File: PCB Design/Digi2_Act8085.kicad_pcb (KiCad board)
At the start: 2 copper layers, 27 parts, among them U1 8085A, U10 8255, U2 Barrel_Jack, U3 L7805, U4 2764, U5 CY6264, U6 74LS373, U7 74LS138, U8 8255, U9 8255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

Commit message: Initial
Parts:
- moved C12 73.7 mm to (141.4, 113.5)
- moved U7 73.7 mm to (172.7, 94.7)
- moved Y1 73.7 mm to (141.4, 101.2)
- moved C2 73.7 mm to (155.2, 96.8)
- moved C4 73.7 mm to (174.8, 122.7)
- moved C5 73.7 mm to (200.5, 111.4)
- moved C6 73.7 mm to (229.1, 111.5)
- moved C9 73.7 mm to (188.9, 100.1)
- moved U1 73.7 mm to (150.1, 101.5)
- moved U4 73.7 mm to (224.7, 116.6)
- moved U5 73.7 mm to (195.3, 116.6)
- moved U8 73.7 mm to (193.4, 105.6)
- moved C3 73.7 mm to (174.0, 89.6)
- moved U6 73.7 mm to (173.2, 126.6)
- moved C7 72.3 mm to (188.8, 48.0)
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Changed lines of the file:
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@@
 	(footprint "Capacitor_THT:C_Disc_D4.3mm_W1.9mm_P5.00mm"
 		(layer "F.Cu")
-		(at 82.81 83.425)
+		(at 155.245 96.8)
 		(descr "C, Disc series, Radial, pin pitch=5.00mm, , diameter*width=4.3*1.9mm^2, Capacitor, http://www.vishay.com/docs/45233/krseries.pdf")
 		(tags "C Disc series Radial pin pitch 5.00mm  diameter 4.3mm width 1.9mm Capacitor")
@@
 	(footprint "Crystal:Crystal_HC49-U_Vertical"
 		(layer "F.Cu")
-		(at 68.925 87.795 -90)
+		(at 141.36 101.17 -90)
 		(descr "Crystal THT HC-49/U http://5hertz.com/pdfs/04404_D.pdf")
 		(tags "THT crystalHC-49/U")
@@
 	(footprint "Package_DIP:DIP-16_W7.62mm_Socket"
 		(layer "F.Cu")
-		(at 100.24 81.36)
+		(at 172.675 94.735)
 		(descr "16-lead though-hole mounted DIP package, row spacing 7.62 mm (300 mils), Socket")
 		(tags "THT DIP DIL PDIP 2.54mm 7.62mm 300mil Socket")
@@
 	(footprint "Package_DIP:DIP-20_W7.62mm_Socket"
 		(layer "F.Cu")
-		(at 100.79 113.27)
+		(at 173.225 126.645)
 		(descr "20-lead though-hole mounted DIP package, row spacing 7.62 mm (300 mils), Socket")
 		(tags "THT DIP DIL PDIP 2.54mm 7.62mm 300mil Socket")
 		(property "Reference" "U6"
-			(at 8.37 -2.72 360)
+			(at 8.37 -2.72 0)
 			(layer "F.SilkS")
 			(effects
@@
 		)
 		(property "Value" "74LS373"
-			(at 7.945 26.37 360)
+			(at 7.945 26.37 0)
 			(layer "F.Fab")
 			(effects
@@
 		)
 		(fp_text user "${REFERENCE}"
-			(at 7.945 12.61 360)
+			(at 7.945 12.61 0)
 			(layer "F.Fab")
 			(effects
@@
 	(footprint "Capacitor_THT:C_Disc_D4.3mm_W1.9mm_P5.00mm"
 		(layer "F.Cu")
-		(at 116.5 86.76 90)
+		(at 188.935 100.135 90)
 		(descr "C, Disc series, Radial, pin pitch=5.00mm, , diameter*width=4.3*1.9mm^2, Capacitor, http://www.vishay.com/docs/45233/krseries.pdf")
 		(tags "C Disc series Radial pin pitch 5.00mm  diameter 4.3mm width 1.9mm Capacitor")
 		(property "Reference" "C9"
-			(at 2.5 -2.2 270)
+			(at 2.5 -2.2 -90)
 			(layer "F.SilkS")
 			(effects
@@
 		)
 		(property "Value" "100nF"
-			(at 2.5 2.2 270)
+			(at 2.5 2.2 -90)
 			(layer "F.Fab")
 			(effects
@@
 		)
 		(fp_text user "${REFERENCE}"
-			(at 2.5 0 270)
+			(at 2.5 0 -90)
 			(layer "F.Fab")
 			(effects
@@
 	(footprint "Package_DIP:DIP-40_W15.24mm"
 		(layer "F.Cu")
-		(at 121.085 48.615 90)
+		(at 193.325 52.115 90)
 		(descr "40-lead though-hole mounted DIP package, row spacing 15.24 mm (600 mils)")
 		(tags "THT DIP DIL PDIP 2.54mm 15.24mm 600mil")
 		(property "Reference" "U10"
-			(at 7.62 -2.33 270)
+			(at 7.62 -2.33 -90)
 			(layer "F.SilkS")
 			(effects
@@
 		)
 		(property "Value" "8255"
-			(at 7.62 50.59 270)
+			(at 7.62 50.59 -90)
 			(layer "F.Fab")
 			(effects
@@
 		)
 		(fp_text user "${REFERENCE}"
-			(at 7.62 24.13 270)
+			(at 7.62 24.13 -90)
 			(layer "F.Fab")
 			(effects
@@
 	(footprint "Capacitor_THT:C_Disc_D4.3mm_W1.9mm_P5.00mm"
 		(layer "F.Cu")
-		(at 101.61 76.27)
+		(at 174.045 89.645)
 		(descr "C, Disc series, Radial, pin pitch=5.00mm, , diameter*width=4.3*1.9mm^2, Capacitor, http://www.vishay.com/docs/45233/krseries.pdf")
 		(tags "C Disc series Radial pin pitch 5.00mm  diameter 4.3mm width 1.9mm Capacitor")
@@
 	(footprint "Package_DIP:DIP-28_W15.24mm_Socket"
 		(layer "F.Cu")
-		(at 122.82 103.225)
+		(at 195.255 116.6)
 		(descr "28-lead though-hole mounted DIP package, row spacing 15.24 mm (600 mils), Socket")
 		(tags "THT DIP DIL PDIP 2.54mm 15.24mm 600mil Socket")
@@
 	(footprint "Package_DIP:DIP-28_W15.24mm"
 		(layer "F.Cu")
-		(at 152.3 103.19)
+		(at 224.735 116.565)
 		(descr "28-lead though-hole mounted DIP package, row spacing 15.24 mm (600 mils)")
 		(tags "THT DIP DIL PDIP 2.54mm 15.24mm 600mil")
@@
 	(footprint "Capacitor_THT:C_Disc_D4.3mm_W1.9mm_P5.00mm"
 		(layer "F.Cu")
-		(at 116.54 65.76 90)
+		(at 188.78 69.26 90)
 		(descr "C, Disc series, Radial, pin pitch=5.00mm, , diameter*width=4.3*1.9mm^2, Capacitor, http://www.vishay.com/docs/45233/krseries.pdf")
 		(tags "C Disc series Radial pin pitch 5.00mm  diameter 4.3mm width 1.9mm Capacitor")
 		(property "Reference" "C8"
-			(at 2.5 -2.2 270)
+			(at 2.5 -2.2 -90)
 			(layer "F.SilkS")
 			(effects
@@
 		)
 		(property "Value" "100nF"
-			(at 2.5 2.2 270)
+			(at 2.5 2.2 -90)
 			(layer "F.Fab")
 			(effects
@@
 		)
 		(fp_text user "${REFERENCE}"
-			(at 2.5 0 270)
+			(at 2.5 0 -90)
 			(layer "F.Fab")
 			(effects
@@
 	(footprint "Capacitor_THT:C_Disc_D4.3mm_W1.9mm_P5.00mm"
 		(layer "F.Cu")
-		(at 128.06 98.07)
+		(at 200.495 111.445)
 		(descr "C, Disc series, Radial, pin pitch=5.00mm, , diameter*width=4.3*1.9mm^2, Capacitor, http://www.vishay.com/docs/45233/krseries.pdf")
 		(tags "C Disc series Radial pin pitch 5.00mm  diameter 4.3mm width 1.9mm Capacitor")
@@
 	(footprint "Package_DIP:DIP-40_W15.24mm"
 		(layer "F.Cu")
-		(at 77.685 88.095)
+		(at 150.12 101.47)
 		(descr "40-lead though-hole mounted DIP package, row spacing 15.24 mm (600 mils)")
 		(tags "THT DIP DIL PDIP 2.54mm 15.24mm 600mil")
@@
 	(footprint "Package_DIP:DIP-40_W15.24mm"
 		(layer "F.Cu")
-		(at 120.94 92.25 90)
+		(at 193.375 105.625 90)
 		(descr "40-lead though-hole mounted DIP package, row spacing 15.24 mm (600 mils)")
 		(tags "THT DIP DIL PDIP 2.54mm 15.24mm 600mil")
 		(property "Reference" "U8"
-			(at 7.62 -2.44 270)
+			(at 7.62 -2.44 -90)
 			(layer "F.SilkS")
 			(effects
@@
 		)
 		(property "Value" "8255"
-			(at 7.62 50.59 270)
+			(at 7.62 50.59 -90)
 			(layer "F.Fab")
 			(effects
@@
 		)
 		(fp_text user "${REFERENCE}"
-			(at 7.62 24.13 270)
+			(at 7.62 24.13 -90)
 			(layer "F.Fab")
 			(effects
@@
 	(footprint "Capacitor_THT:C_Disc_D4.3mm_W1.9mm_P5.00mm"
 		(layer "F.Cu")
-		(at 68.925 100.092349 -90)
+		(at 141.36 113.467349 -90)
 		(descr "C, Disc series, Radial, pin pitch=5.00mm, , diameter*width=4.3*1.9mm^2, Capacitor, http://www.vishay.com/docs/45233/krseries.pdf")
 		(tags "C Disc series Radial pin pitch 5.00mm  diameter 4.3mm width 1.9mm Capacitor")
@@
 	(footprint "Package_DIP:DIP-40_W15.24mm"
 		(layer "F.Cu")
-		(at 120.99 71.25 90)
+		(at 193.23 74.75 90)
 		(descr "40-lead though-hole mounted DIP package, row spacing 15.24 mm (600 mils)")
 		(tags "THT DIP DIL PDIP 2.54mm 15.24mm 600mil")
 		(property "Reference" "U9"
-			(at 7.62 -2.33 270)
+			(at 7.62 -2.33 -90)
 			(layer "F.SilkS")
 			(effects
@@
 		)
 		(property "Value" "8255"
-			(at 7.62 50.59 270)
+			(at 7.62 50.59 -90)
 			(layer "F.Fab")
 			(effects
@@
 		)
 		(fp_text user "${REFERENCE}"
-			(at 7.62 24.13 270)
+			(at 7.62 24.13 -90)
 			(layer "F.Fab")
 			(effects
@@
 	(footprint "Capacitor_THT:C_Disc_D4.3mm_W1.9mm_P5.00mm"
 		(layer "F.Cu")
-		(at 102.41 109.3)
+		(at 174.845 122.675)
 		(descr "C, Disc series, Radial, pin pitch=5.00mm, , diameter*width=4.3*1.9mm^2, Capacitor, http://www.vishay.com/docs/45233/krseries.pdf")
 		(tags "C Disc series Radial pin pitch 5.00mm  diameter 4.3mm width 1.9mm Capacitor")
 		(property "Reference" "C4"
-			(at 2.18 -5.355 360)
+			(at 2.18 -5.355 0)
 			(layer "F.SilkS")
 			(effects
@@
 		)
 		(property "Value" "100nF"
-			(at 2.5 2.2 360)
+			(at 2.5 2.2 0)
 			(layer "F.Fab")
 			(effects
@@
 		)
 		(fp_text user "${REFERENCE}"
-			(at 2.5 0 360)
+			(at 2.5 0 0)
 			(layer "F.Fab")
 			(effects
@@
 	(footprint "Capacitor_THT:C_Disc_D4.3mm_W1.9mm_P5.00mm"
 		(layer "F.Cu")
-		(at 156.675 98.115)
+		(at 229.11 111.49)
 		(descr "C, Disc series, Radial, pin pitch=5.00mm, , diameter*width=4.3*1.9mm^2, Capacitor, http://www.vishay.com/docs/45233/krseries.pdf")
 		(tags "C Disc series Radial pin pitch 5.00mm  diameter 4.3mm width 1.9mm Capacitor")
@@
 	(footprint "Capacitor_THT:C_Disc_D4.3mm_W1.9mm_P5.00mm"
 		(layer "F.Cu")
-		(at 116.54 44.51 90)
+		(at 188.78 48.01 90)
 		(descr "C, Disc series, Radial, pin pitch=5.00mm, , diameter*width=4.3*1.9mm^2, Capacitor, http://www.vishay.com/docs/45233/krseries.pdf")
 		(tags "C Disc series Radial pin pitch 5.00mm  diameter 4.3mm width 1.9mm Capacitor")
 		(property "Reference" "C7"
-			(at 2.5 -2.55 270)
+			(at 2.5 -2.55 -90)
 			(layer "F.SilkS")
 			(effects
@@
 		)
 		(property "Value" "100nF"
-			(at 2.5 2.2 270)
+			(at 2.5 2.2 -90)
 			(layer "F.Fab")
 			(effects
@@
 		)
 		(fp_text user "${REFERENCE}"
-			(at 2.5 0 270)
+			(at 2.5 0 -90)
 			(layer "F.Fab")
 			(effects
@@
 	)
 	(segment
-		(start 92.925 88.095)
-		(end 94.255 89.425)
+		(start 165.36 101.47)
+		(end 166.69 102.8)
 		(width 0.2)
 		(layer "F.Cu")

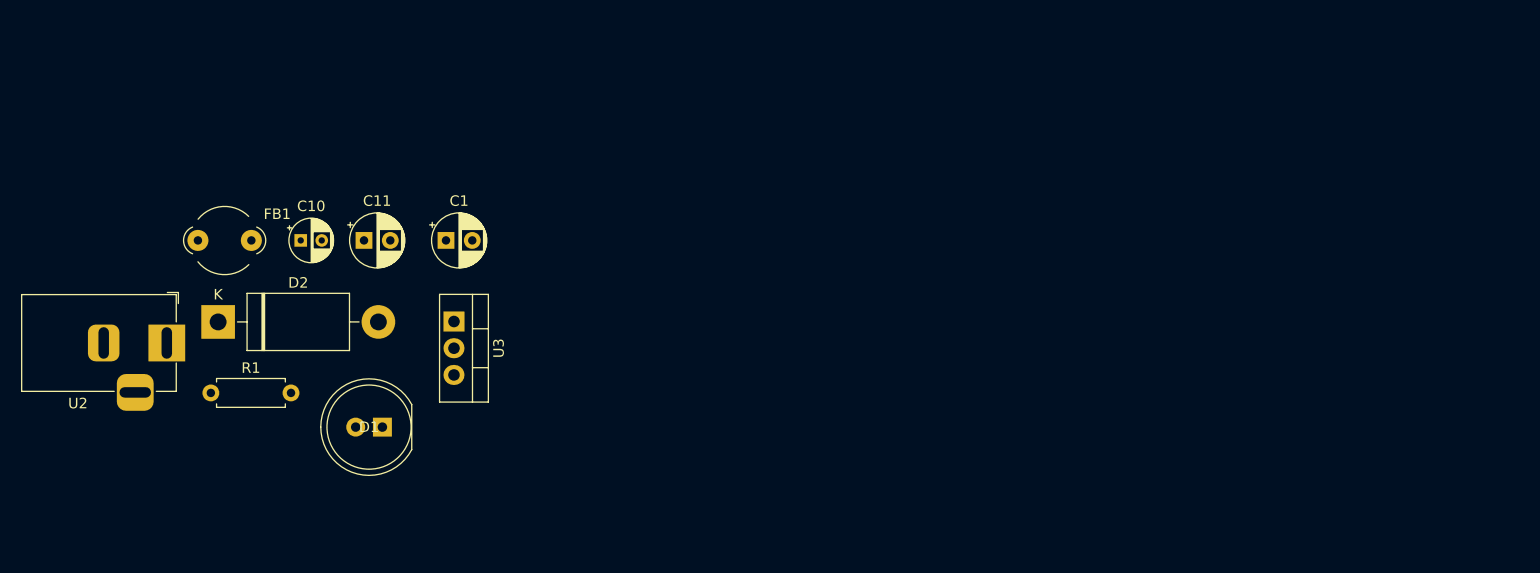
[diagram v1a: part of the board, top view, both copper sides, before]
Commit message: Set Pre defined width
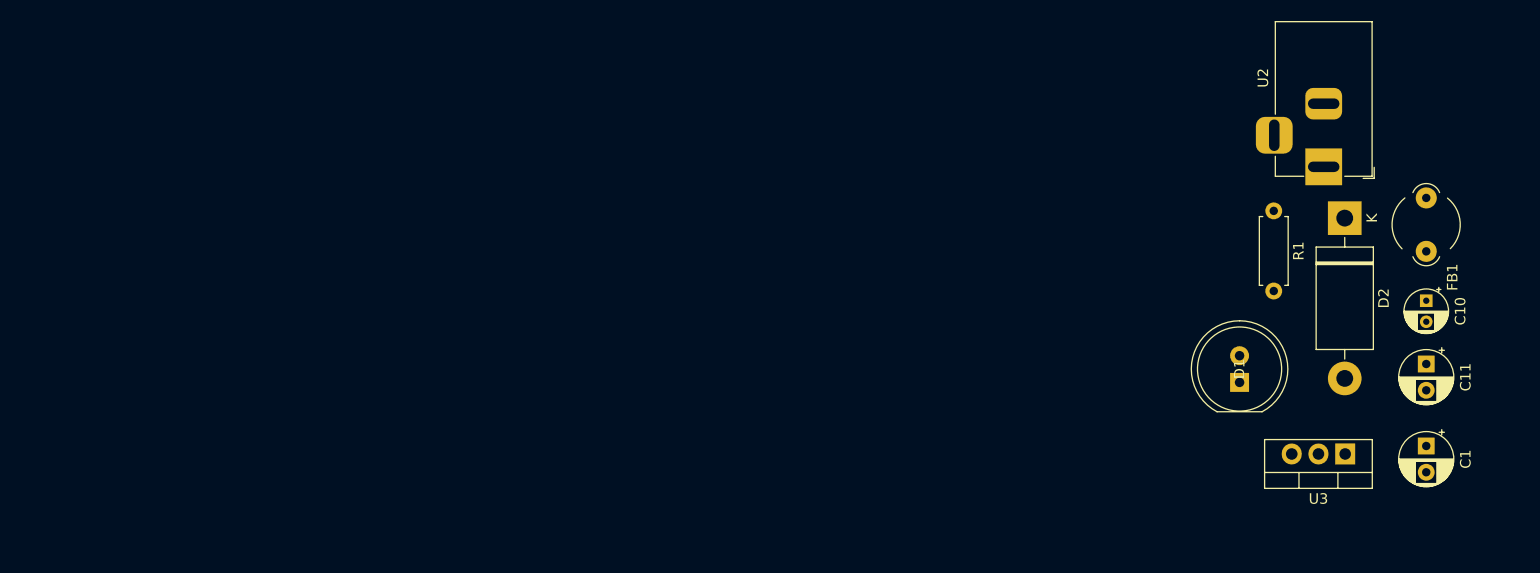
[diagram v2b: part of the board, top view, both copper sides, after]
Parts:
- moved FB1 111.7 mm to (162.2, 48.5), turned to 90 degrees
- moved U2 111.3 mm to (152.5, 40.5), turned to -90 degrees
- moved D2 107.6 mm to (154.5, 45.4), turned to -90 degrees
- moved C10 107.2 mm to (162.2, 53.2), turned to -90 degrees
- moved R1 102.5 mm to (147.8, 44.7), turned to -90 degrees
- moved C11 101.7 mm to (162.2, 59.2), turned to -90 degrees
- moved C1 95.2 mm to (162.2, 67.0), turned to -90 degrees
- moved U3 85.7 mm to (154.5, 67.8), turned to 180 degrees
- moved D1 81.6 mm to (144.5, 61.0), turned to 90 degrees

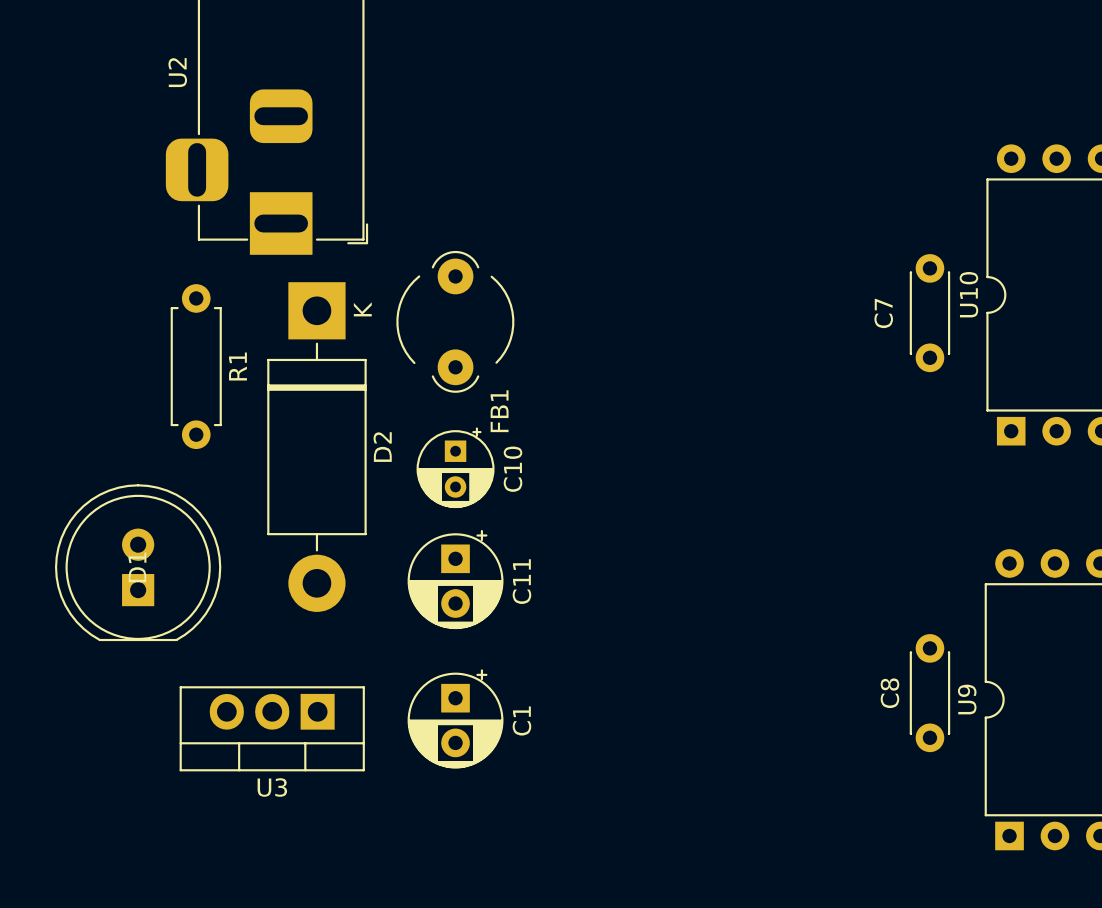
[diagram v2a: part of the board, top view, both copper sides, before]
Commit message: power supply routing
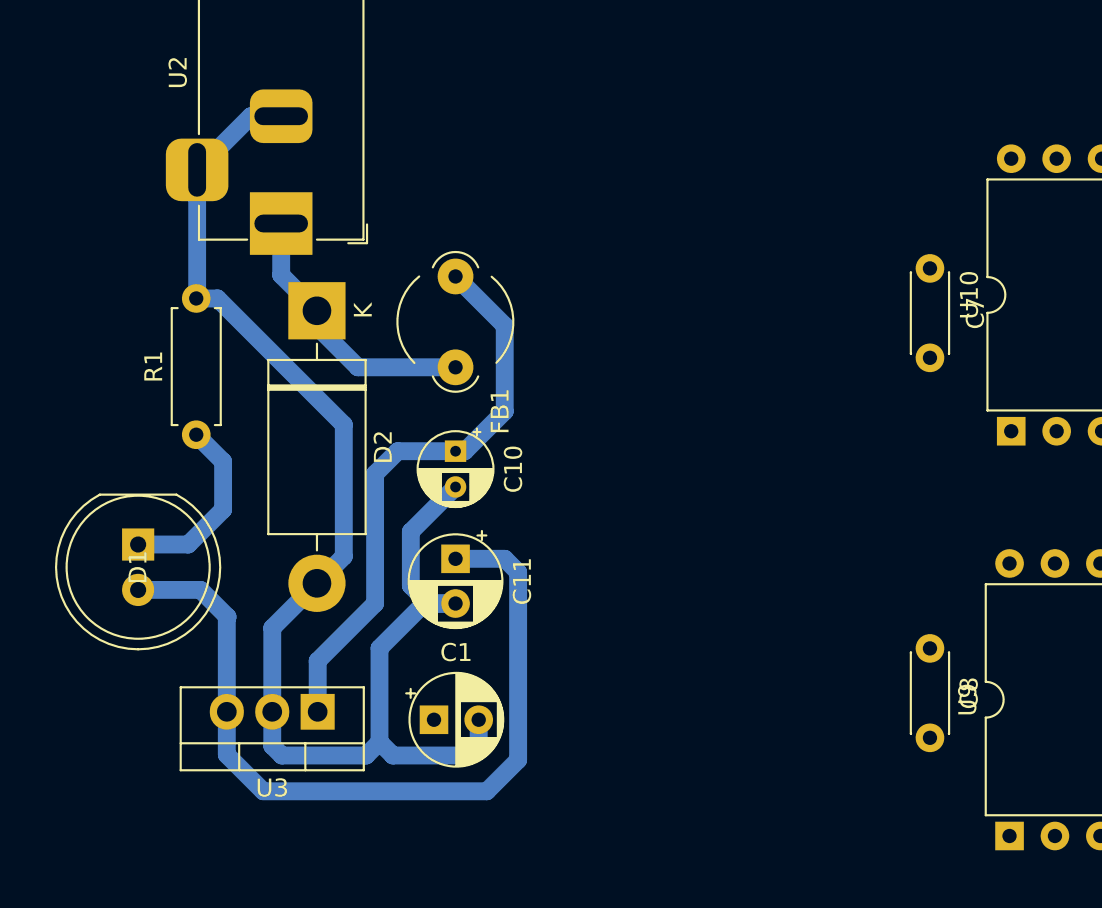
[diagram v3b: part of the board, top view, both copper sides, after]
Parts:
- moved R1 7.62 mm to (147.8, 52.3), turned to 90 degrees
- moved C7 5.00 mm to (188.8, 43.0), turned to -90 degrees
- moved C8 5.00 mm to (188.8, 64.3), turned to -90 degrees
- moved D1 2.55 mm to (144.5, 58.5), turned to -90 degrees
- moved C1 1.70 mm to (161.0, 68.2), turned to 0 degrees
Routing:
- net GND: track 0.00 -> 78.0 mm
- net +5V: track 1.88 -> 47.4 mm
- net Net-(U3-IN): track 0.00 -> 32.1 mm
- net Net-(D2-K): track 0.00 -> 15.3 mm
- net Net-(D1-K): track 0.00 -> 10.4 mm

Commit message: copy of main
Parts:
- moved C1 3.79 mm to (157.3, 67.7)
- moved D1 3.79 mm to (140.8, 57.9)
- moved U3 3.79 mm to (150.8, 67.3)
- moved C10 3.79 mm to (158.5, 52.7)
- moved C11 3.79 mm to (158.5, 58.7)
- moved D2 3.79 mm to (150.8, 44.8)
- moved FB1 3.79 mm to (158.5, 48.0)
- moved R1 3.79 mm to (144.0, 51.8)
- moved U2 3.79 mm to (148.8, 40.0)

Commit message: test5
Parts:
- moved FB1 108.0 mm to (50.5, 47.5), turned to 180 degrees
- moved U2 107.6 mm to (42.5, 57.2), turned to 0 degrees
- moved D2 103.9 mm to (47.4, 55.2), turned to 0 degrees
- moved C10 103.4 mm to (55.2, 47.5), turned to 0 degrees
- moved C11 97.9 mm to (61.2, 47.5), turned to 0 degrees
- moved R1 97.8 mm to (46.7, 62.0), turned to 0 degrees
- moved C1 90.5 mm to (69.0, 47.5)
- moved C12 88.0 mm to (53.5, 108.8)
- moved Y1 88.0 mm to (53.5, 96.5)
- moved U1 88.0 mm to (62.3, 96.9)
- moved C6 86.2 mm to (143.1, 106.3)
- moved U4 86.2 mm to (138.7, 111.3)
- moved U5 83.7 mm to (111.7, 111.4)
- moved C2 83.0 mm to (72.4, 92.2), turned to 180 degrees
- moved U6 82.2 mm to (91.1, 122.0)
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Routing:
- net /Memory and Peripheral Inteface/AD1: track 0.00 -> 302.6 mm, vias 0 -> 3
- net /Memory and Peripheral Inteface/AD2: track 0.00 -> 287.0 mm, vias 0 -> 1
- net GND: track 78.0 -> 349.3 mm, vias 0 -> 5
- net +5V: track 47.4 -> 318.0 mm
- net /Memory and Peripheral Inteface/AD3: track 0.00 -> 243.2 mm, vias 0 -> 1
- net /Memory and Peripheral Inteface/AD0: track 0.00 -> 231.6 mm, vias 0 -> 2
- net /Memory and Peripheral Inteface/AD6: track 0.00 -> 199.8 mm, vias 0 -> 1
- net /Memory and Peripheral Inteface/AD7: track 0.00 -> 191.6 mm, vias 0 -> 1
- net /Memory and Peripheral Inteface/AD4: track 0.00 -> 181.6 mm, vias 0 -> 2
- net /Memory and Peripheral Inteface/~{WR}: track 0.00 -> 178.2 mm, vias 0 -> 1
- net /Memory and Peripheral Inteface/AD5: track 0.00 -> 175.7 mm, vias 0 -> 2
- net /Memory and Peripheral Inteface/A12: track 0.00 -> 135.9 mm, vias 0 -> 1
- net /Memory and Peripheral Inteface/A0: track 0.00 -> 103.3 mm
- net /Memory and Peripheral Inteface/A8: track 0.00 -> 96.8 mm
- net /Memory and Peripheral Inteface/A2: track 0.00 -> 94.8 mm, vias 0 -> 1
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
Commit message: testxxx
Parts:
- moved R1 106.7 mm to (153.3, 56.0), turned to 180 degrees
- moved C1 100.3 mm to (169.2, 42.7), turned to 90 degrees
- moved C11 99.1 mm to (160.2, 41.5)
- moved D2 99.1 mm to (146.3, 49.3)
- moved FB1 99.1 mm to (149.5, 41.5)
- moved U2 99.1 mm to (141.5, 51.3)
- moved C10 99.1 mm to (154.2, 41.5)
- moved U3 99.1 mm to (168.8, 49.2)
- moved D1 96.6 mm to (159.4, 59.3), turned to 0 degrees
- moved C12 88.0 mm to (141.4, 113.5)
- moved Y1 88.0 mm to (141.4, 101.2)
- moved U1 88.0 mm to (150.1, 101.5)
- moved C6 86.2 mm to (229.1, 111.5)
- moved U4 86.2 mm to (224.7, 116.6)
- moved U5 83.7 mm to (195.3, 116.6)
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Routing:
- net /Memory and Peripheral Inteface/AD1: track 302.6 -> 0.00 mm, vias 3 -> 0
- net /Memory and Peripheral Inteface/AD2: track 287.0 -> 0.00 mm, vias 1 -> 0
- net GND: track 349.3 -> 78.0 mm, vias 5 -> 0
- net +5V: track 318.0 -> 47.4 mm
- net /Memory and Peripheral Inteface/AD3: track 243.2 -> 0.00 mm, vias 1 -> 0
- net /Memory and Peripheral Inteface/AD0: track 231.6 -> 0.00 mm, vias 2 -> 0
- net /Memory and Peripheral Inteface/AD6: track 199.8 -> 0.00 mm, vias 1 -> 0
- net /Memory and Peripheral Inteface/AD7: track 191.6 -> 0.00 mm, vias 1 -> 0
- net /Memory and Peripheral Inteface/AD4: track 181.6 -> 0.00 mm, vias 2 -> 0
- net /Memory and Peripheral Inteface/~{WR}: track 178.2 -> 0.00 mm, vias 1 -> 0
- net /Memory and Peripheral Inteface/AD5: track 175.7 -> 0.00 mm, vias 2 -> 0
- net /Memory and Peripheral Inteface/A12: track 135.9 -> 0.00 mm, vias 1 -> 0
- net /Memory and Peripheral Inteface/A0: track 103.3 -> 0.00 mm
- net /Memory and Peripheral Inteface/A8: track 96.8 -> 0.00 mm
- net /Memory and Peripheral Inteface/A2: track 94.8 -> 0.00 mm, vias 1 -> 0
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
